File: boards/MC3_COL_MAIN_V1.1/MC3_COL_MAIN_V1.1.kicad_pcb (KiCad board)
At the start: 4 copper layers, 66 x 66 mm, 157 parts, among them J1 SUPPLY_IN, J10 MOTOR, J11 MOTOR, J12 CAN, J13 HARNESS_FFC_6P, J2 SWD, J3 ENC_leaf1, J4 ENC_leaf2, J5 ENC_leaf3, J6 ENC_leaf4, J7 MOTOR, J8 MOTOR, J9 MOTOR, Q1 AO4421, SW1 SKRKAEE020, U1 AMS1117-3.3, U10 GP1S094HCZ0F, U11 GP1S094HCZ0F, U12 LM61460AANRJRR, U2 STM32U595RJT6, U3 DRV8214RTER, U4 DRV8214RTER, U5 DRV8214RTER, U6 DRV8214RTER, U7 DRV8214RTER, U8 TJA1051T/3, U9 AEDR-8300-1Q0, Y1 8MHz

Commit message: V1.1: encoder FFC VIN on filtered VSENS, motor pads off MotorChannel, yaw nets renamed
- Connectors: encoder FFC VIN now fed from VSENS (VM through FB61 + C63);
  ENC_leaf1-4 / RC_OUT labels re-placed; SIG pull-ups to +3V3 noted on sheet
- MotorChannel: J7-J9 MOTOR pad connectors (Conn_01x02) and their OUT1/OUT2
  hierarchical labels removed from the shared sheet
- MCU: ENC_leaf1-4 global labels re-placed; sheet notes carried over
- Root: H5 SLOT-PASSTHRU mounting hole removed
- PCB: yaw motor nets YAW_OUT* -> /yaw/OUT*; CANH/CANL pad assignment swapped;
  VSENS/VM net reassignments and follow-up routing (~106 segments, 12 vias,
  zone edits) to match the schematic

Co-Authored-By: Claude Fable 5 <noreply@anthropic.com>
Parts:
- removed H5: SLOT-PASSTHRU, MC3_COL_MAIN:SlotNPTH_PassThrough
- removed J11: MOTOR, MC3_COL_MAIN:SolderPads_2x_2.2x1.4mm_P2.6mm
- moved H4 10.8 mm to (119.1, 77.0)
- moved TP6 7.43 mm to (110.3, 74.1)
- moved J12 3.53 mm to (122.0, 86.3), turned to 0 degrees
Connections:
- J12 pad 1: CANL -> CANH
- J12 pad 2: CANH -> CANL
- U7 pad 6: YAW_OUT1 -> /yaw/OUT1
- U7 pad 8: YAW_OUT2 -> /yaw/OUT2
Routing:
- net RC_OUT_leaf1: track 28.7 -> 55.9 mm, vias 3 -> 5
- net IPROPI_leaf1: track 82.8 -> 58.0 mm, vias 2 -> 4
- net RC_OUT_leaf3: track 43.3 -> 61.7 mm, vias 2 -> 3
- net RC_OUT_leaf2: track 50.6 -> 67.9 mm, vias 4 -> 5
- net CANH: track 79.1 -> 76.3 mm
- net /MCU/YAW_LIM: track 34.6 -> 37.2 mm
- net PH_leaf2: track 35.9 -> 38.0 mm
- net CANL: track 66.7 -> 64.9 mm
- net VSENS: track 49.8 -> 48.2 mm
- net Net-(U11-A): track 9.34 -> 10.2 mm
- net VM: track 188.5 -> 187.9 mm
- net EN_leaf1: track 47.4 -> 47.9 mm
- net GND: vias 37 -> 36
- net ENC_leaf2: vias 2 -> 3
- net ENC_leaf1: vias 3 -> 2

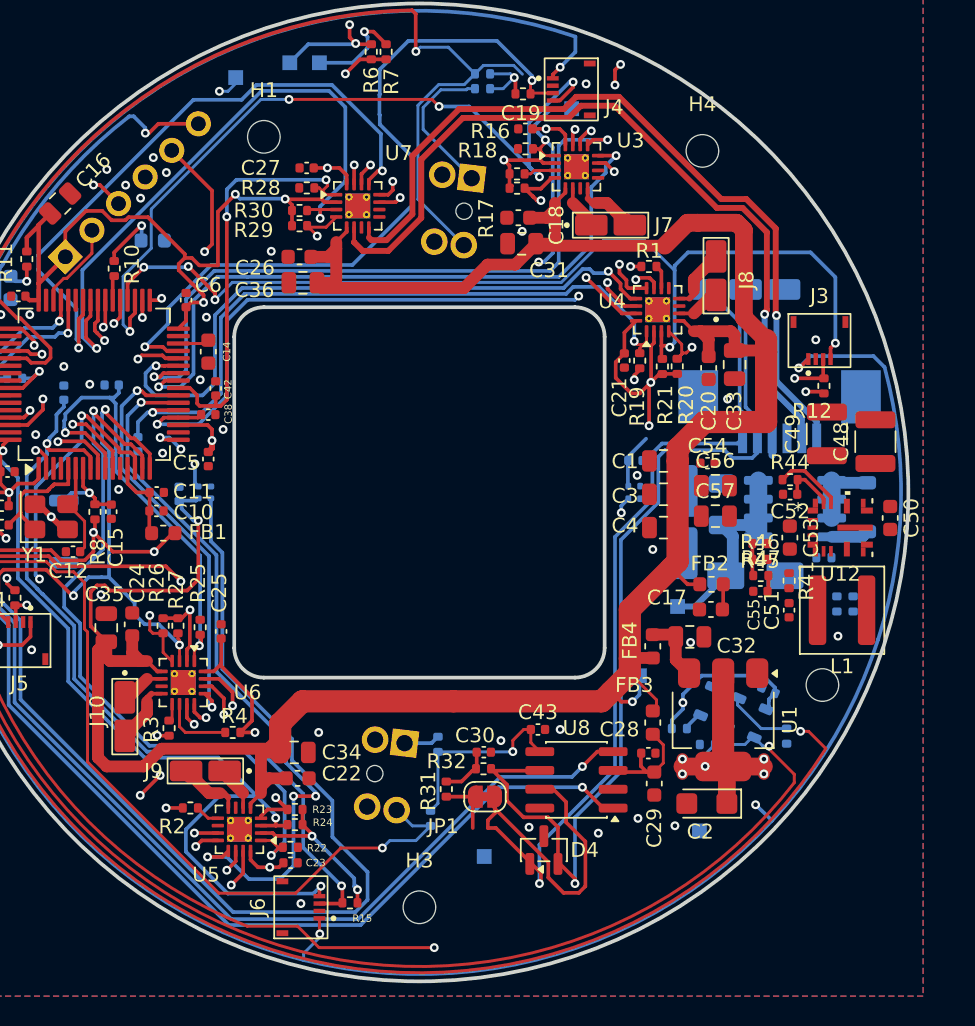
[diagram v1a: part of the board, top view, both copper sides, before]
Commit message: V1.1: power routing pass — 24V chain + buck routed, stale-net/short fixes, VQFN corner pads fused, yaw OUT hier labels restored
- Board: VIN chain and buck cell routed (VIN_SW vias at Q1 source, SW between
  pads 8/9, boot via In2); ENC_leaf1 via at (83.9,97.075) renamed to ENC_leaf2;
  stray GND via under U1 strap deleted; VSENS via moved off the R32 rim arc;
  YAW_ENC_B gap closed at U9.1.
- MotorChannel.kicad_sch: OUT1/OUT2 hierarchical labels (passive) restored on
  the driver output wires; netlist verified YAW_OUT1/2 = U7 OUT + J13 5/6.
- VQFN-HR14_RJR_TEX: UL corner L-extensions were net-less F.Cu polygons over
  pads 1/5/9/11 (DRC overlap noise, parser-breaking width-0 strokes); fused
  into single rect pads covering the exact union; polys deleted. Board still
  carries the old embedded copy - Update Footprint on U12 pending.

Co-Authored-By: Claude Fable 5 <noreply@anthropic.com>
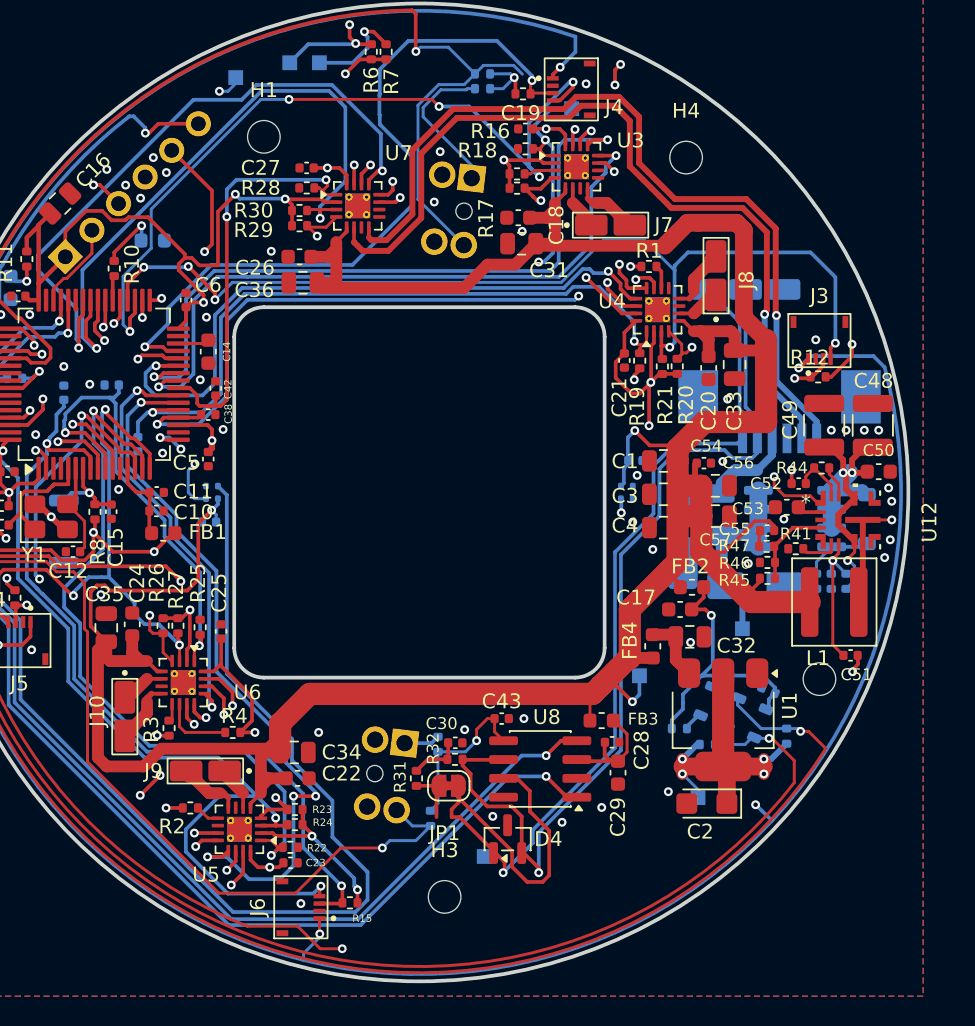
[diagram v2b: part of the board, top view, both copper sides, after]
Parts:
- moved C51 5.15 mm to (129.1, 111.0), turned to 0 degrees
- moved TP2 4.62 mm to (121.8, 109.2)
- moved C55 4.12 mm to (123.5, 102.6), turned to 180 degrees
- moved FB3 3.45 mm to (112.3, 115.4), turned to 0 degrees
- moved C50 3.22 mm to (131.0, 98.6), turned to 0 degrees
- moved C44 2.78 mm to (85.8, 102.0), turned to 180 degrees
- moved D4 2.56 mm to (106.0, 123.4)
- moved C28 2.56 mm to (113.0, 116.9)
- moved C29 2.56 mm to (113.4, 118.9)
- moved C43 2.56 mm to (105.6, 115.3)
- moved JP1 2.56 mm to (102.0, 119.8)
- moved U8 2.56 mm to (108.2, 118.7)
- moved R45 2.40 mm to (123.5, 105.8), turned to 0 degrees
- moved R44 2.28 mm to (127.2, 98.3), turned to 180 degrees
- moved TP3 2.25 mm to (118.8, 120.6)
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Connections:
- U7 pad 6: /yaw/OUT1 -> YAW_OUT1
- U7 pad 8: /yaw/OUT2 -> YAW_OUT2
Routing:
- net VM: track 187.9 -> 228.5 mm, vias 2 -> 4
- net BUCK_SYNC: track 51.6 -> 13.8 mm, vias 1 -> 2
- net /Power/VIN_SW: track 5.01 -> 23.7 mm, vias 0 -> 3
- net /Power/BUCK_SW: track 0.00 -> 16.9 mm, vias 0 -> 2
- net /Power/BUCK_EN: track 0.00 -> 10.4 mm, vias 0 -> 1
- net VSENS: track 48.2 -> 54.9 mm
- net +3V3: track 208.6 -> 213.9 mm
- net VIN_PAD: track 3.97 -> 8.70 mm
- net /Power/BUCK_FB: track 2.18 -> 5.83 mm
- net /Power/BUCK_RT: track 0.00 -> 2.58 mm
- net Net-(U12-RBOOT): track 4.70 -> 2.17 mm
- net /Power/Q1_G: track 2.54 -> 4.71 mm
- net CAN1_RX: track 84.2 -> 82.0 mm
- net CAN1_TX: track 84.3 -> 82.2 mm
- net YAW_OUT2: track 53.6 -> 55.6 mm
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
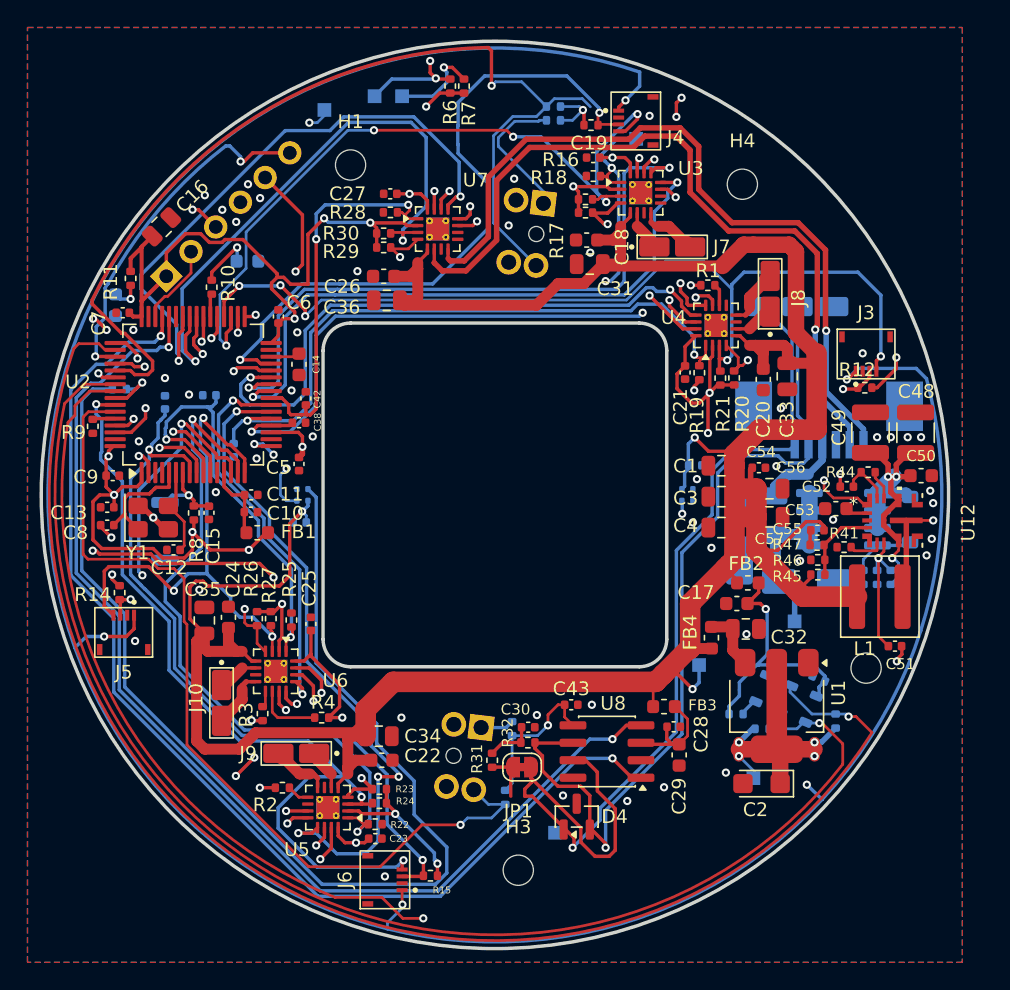
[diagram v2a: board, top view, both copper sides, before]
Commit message: Vault consolidation: Main-Board-02 rung folded back into Main-Board-01
Nothing was built at V1.0, so the 24 V revision never justified a rung bump.
Main-Board-01 now builds boards/MC3_COL_MAIN_V1.1 (24 V input); V1.0 stays in
the repo as the 5 V-only fallback revision. Repo side: CLAUDE.md rung mapping,
MIGRATION.md header and §14 pointer, LM61460 layout-note link. Vault side
(edited directly): Main-Board-01 Power rewritten as the 24 V chain, rung page
carries the V1.0→V1.1 delta/BOM/gates, Main-Board-02 folder deleted, 13 pages'
references rewritten.

Co-Authored-By: Claude Fable 5 <noreply@anthropic.com>
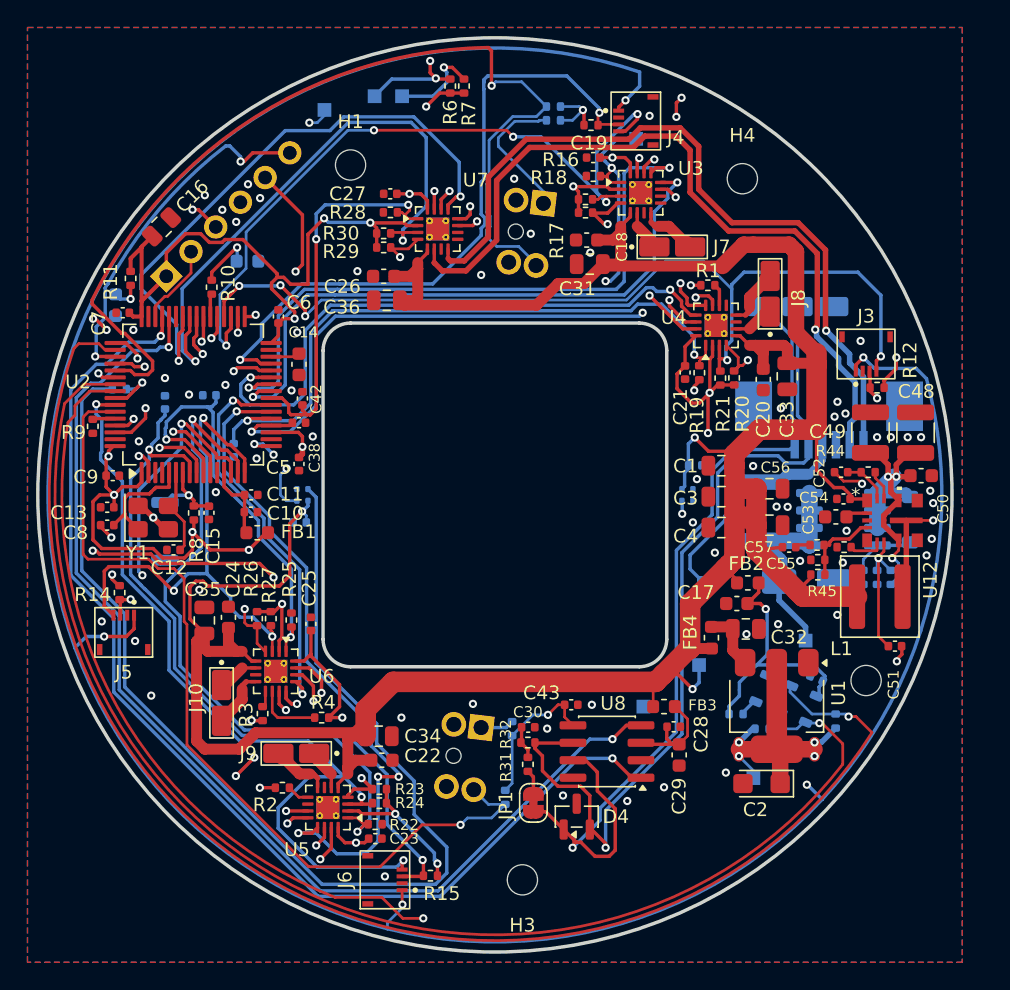
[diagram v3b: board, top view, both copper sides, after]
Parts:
- removed J1: SUPPLY_IN, MC3_COL_MAIN:SolderPads_2x_3.5x2.0mm_P4.2mm
- added TP9: VIN_PAD, MC3_COL_MAIN:TestPoint_Pad_1.0x1.0mm, B.Cu at (115.2, 106.4)
- F1: footprint MC3_COL_MAIN:Fuse_1206_3216Metric -> MC3_COL_MAIN:Fuse_1812_4532Metric
- moved TP7 11.2 mm to (110.8, 115.4)
- moved C54 6.56 mm to (125.4, 100.3), turned to 180 degrees
- moved JP1 2.73 mm to (102.8, 122.4), turned to 90 degrees
- moved R31 2.62 mm to (102.4, 119.6)
- moved C55 2.40 mm to (121.4, 103.8), turned to 0 degrees
- moved TP2 1.61 mm to (122.6, 110.6)
- moved F1 1.23 mm to (119.2, 101.2)
- moved C52 1.13 mm to (125.2, 98.3)
- moved H2 0.90 mm to (127.0, 113.5)
- moved R12 0.89 mm to (127.8, 92.2)
- moved H3 0.76 mm to (102.0, 128.0)
- moved C57 0.60 mm to (120.0, 102.2)
- moved C53 0.60 mm to (124.8, 101.6)
- moved H4 0.40 mm to (118.0, 77.0)
- moved C42 0.25 mm to (86.0, 93.0)
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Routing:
- net VM: track 228.5 -> 215.4 mm, vias 4 -> 3
- net CANH: track 76.0 -> 66.1 mm
- net VIN_PAD: track 8.70 -> 16.1 mm
- net VIN_PROT: track 13.4 -> 16.7 mm
- net ENC_leaf2: track 79.6 -> 82.2 mm
- net /MCU/YAW_LIM: track 37.2 -> 35.1 mm
- net /CAN/TERM_H: track 3.72 -> 1.81 mm
- net ENC_leaf1: track 49.9 -> 48.2 mm
- net /CAN/TERM_MID: track 3.55 -> 2.42 mm
- net +3V3: track 213.9 -> 212.9 mm
- net VSENS: track 54.9 -> 54.0 mm
- net GND: vias 49 -> 62
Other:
- board size 66 x 66 mm -> 66.5 x 66.5 mm
